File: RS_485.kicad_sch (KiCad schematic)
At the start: 17 parts, among them U6 SP3071EEN-L/TR

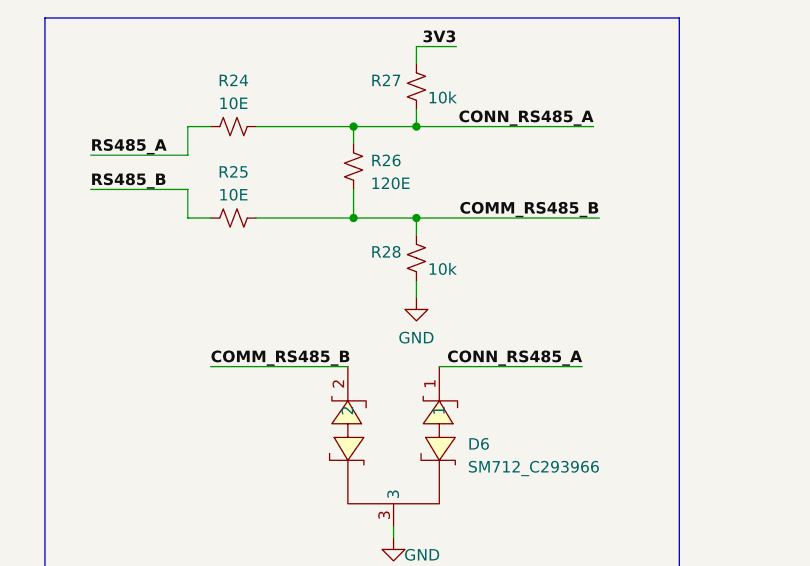
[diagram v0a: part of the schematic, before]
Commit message: Completed RS485 and CAN routing
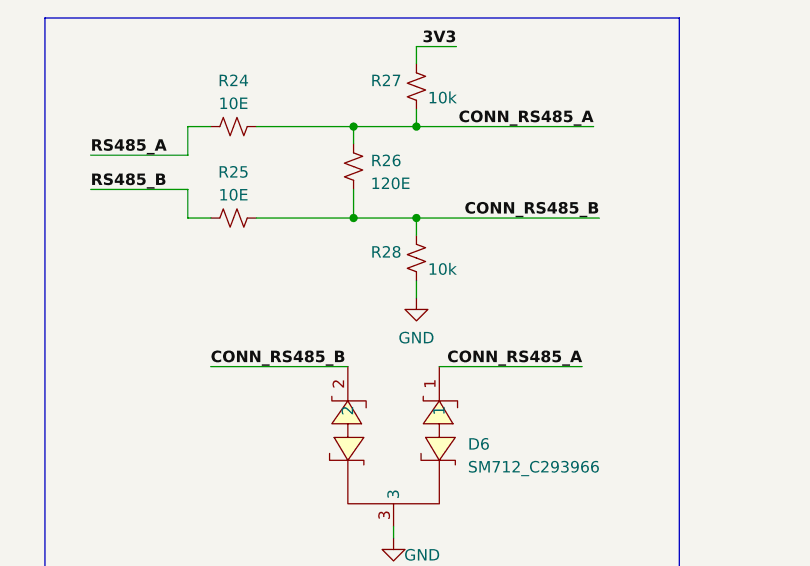
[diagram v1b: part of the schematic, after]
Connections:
- net COMM_RS485_B is gone; now on net CONN_RS485_B: D6.2, R25.2, R26.1, R28.2
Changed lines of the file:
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@@
     (effects (font (size 1.27 1.27) (thickness 0.254) bold (color 255 0 0 1)) (justify right bottom))
   )
-  (label "COMM_RS485_B" (at 262.89 81.28 180) (fields_autoplaced)
+  (label "CONN_RS485_B" (at 262.89 81.28 180) (fields_autoplaced)
     (effects (font (size 1.27 1.27) (thickness 0.254) bold (color 0 0 0 1)) (justify right bottom))
   )
@@
     (effects (font (size 1.27 1.27) (thickness 0.254) bold (color 0 0 255 1)) (justify right bottom))
   )
-  (label "COMM_RS485_B" (at 219.71 97.79 0) (fields_autoplaced)
+  (label "CONN_RS485_B" (at 219.71 97.79 0) (fields_autoplaced)
     (effects (font (size 1.27 1.27) (thickness 0.254) bold (color 0 0 0 1)) (justify left bottom))
   )

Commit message: Merge changes upstream
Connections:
- net CONN_RS485_A renamed RS485_P
- net CONN_RS485_B renamed RS485_N
- net RS485_A renamed RS_485_P
- net RS485_B renamed RS_485_N
- net RS485_~{RE}_DE renamed RS_485_~{RE}_DE
- net RS_485_DI renamed RS_485_TX
- net RS_485_RO renamed RS_485_RX
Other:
- moved on the sheet: D6

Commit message: Added HW-Tinkerers logo and supporting graphics
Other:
- company: (none) -> HW-TINKERERS (hw.tinkerers@gmail.com)
- title: (none) -> HARDWARE TINKERERS ESP32-S3 DB
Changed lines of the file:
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@@
 (kicad_sch (version 20230121) (generator eeschema)
   (paper "A4")
+  (title_block
+    (title "HARDWARE TINKERERS ESP32-S3 DB")
+    (rev "1.0.0")
+    (company "HW-TINKERERS (hw.tinkerers@gmail.com)")
+    (comment 1 "Email: bhandarkasrishtikr111@gmail.com")
+    (comment 2 "Author: Srishtik Bhandarkar")
+    (comment 3 "Email: vaibhavkhatri00@gmail.com")
+    (comment 4 "Author: Vaibhav Khatri")
+    (comment 5 "Official HW-Tinkerers email: hw.tinkerers@gmail.com")
+  )
   (junction (at 242.57 71.12) (diameter 0) (color 0 0 0 0)
   )

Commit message: Added production files for JLC (BOM and CPL)
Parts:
- C22: LCSC Part Number (none) -> C2173920
- D6: LCSC Part Number (none) -> C293966
- R13: LCSC Part Number (none) -> C95177
- R24, R25, R30, R31: LCSC Part Number (none) -> C102753
- R26: LCSC Part Number (none) -> C114758
- R27, R28, R29: LCSC Part Number (none) -> C60490
- R32, R33: LCSC Part Number (none) -> C105872
- TP1, TP2, TP5: now left out of the parts list
- U6: LCSC Part Number (none) -> C28746; PN (none) -> SP3071EEN-L/TR
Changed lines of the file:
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@@
+      (effects (font (size 1.27 1.27)) hide)
+    )
+    (property "LCSC Part Number" "C102753" (at 58.42 93.345 0)
       (effects (font (size 1.27 1.27)) hide)
     )
@@
       (effects (font (size 1.27 1.27)) hide)
     )
+    (property "LCSC Part Number" "C102753" (at 58.42 101.6 0)
+      (effects (font (size 1.27 1.27)) hide)
+    )
     (pin "1")
     (pin "2")
@@
       (effects (font (size 1.27 1.27)) hide)
     )
+    (property "LCSC Part Number" "C102753" (at 222.25 71.12 0)
+      (effects (font (size 1.27 1.27)) hide)
+    )
     (pin "1")
     (pin "2")
@@
       (effects (font (size 1.27 1.27)) hide)
     )
+    (property "LCSC Part Number" "C114758" (at 235.585 75.565 0)
+      (effects (font (size 1.27 1.27)) hide)
+    )
     (pin "1")
     (pin "2")
@@
       (effects (font (size 1.27 1.27)) hide)
     )
+    (property "LCSC Part Number" "C60490" (at 242.57 66.675 0)
+      (effects (font (size 1.27 1.27)) hide)
+    )
     (pin "1")
     (pin "2")
@@
       (effects (font (size 1.27 1.27)) hide)
     )
+    (property "LCSC Part Number" "C102753" (at 222.25 81.28 0)
+      (effects (font (size 1.27 1.27)) hide)
+    )
     (pin "1")
     (pin "2")
@@
   )
   (symbol (lib_id "ESP32-S3_DB:TestPoint_Alt") (at 46.99 101.6 0) (unit 1)
-    (in_bom yes) (on_board yes) (dnp no)
+    (in_bom no) (on_board yes) (dnp no)
     (property "Reference" "TP2" (at 42.545 98.425 0)
       (effects (font (size 1.27 1.27)) (justify left))
@@
       (effects (font (size 1.27 1.27)) hide)
     )
+    (property "Sim.Enable" "0" (at 46.99 101.6 0)
+      (effects (font (size 1.27 1.27)) hide)
+    )
     (pin "1")
     (instances
@@
       (effects (font (size 1.27 1.27)) hide)
     )
+    (property "LCSC Part Number" "C95177" (at 175.26 70.485 0)
+      (effects (font (size 1.27 1.27)) hide)
+    )
     (pin "1")
     (pin "2")
@@
       (effects (font (size 1.27 1.27)) hide)
     )
+    (property "LCSC Part Number" "C293966" (at 236.22 107.95 0)
+      (effects (font (size 1.27 1.27)) hide)
+    )
     (pin "1")
     (pin "2")
@@
     (property "Arrow Price/Stock" "https://www.arrow.com/en/products/max485esat/maxim-integrated?region=nac" (at 161.29 1080.01 0)
       (effects (font (size 1.27 1.27)) (justify left top) hide)
+    )
+    (property "LCSC Part Number" "C28746" (at 139.7 85.09 0)
+      (effects (font (size 1.27 1.27)) hide)
+    )
+    (property "PN" "SP3071EEN-L/TR" (at 139.7 85.09 0)
+      (effects (font (size 1.27 1.27)) hide)
     )
     (pin "1")
@@
       (effects (font (size 1.27 1.27)) hide)
     )
+    (property "LCSC Part Number" "C105872" (at 69.215 85.725 0)
+      (effects (font (size 1.27 1.27)) hide)
+    )
     (pin "1")
     (pin "2")
@@
       (effects (font (size 1.27 1.27)) hide)
     )
+    (property "LCSC Part Number" "C2173920" (at 170.815 76.835 0)
+      (effects (font (size 1.27 1.27)) hide)
+    )
     (pin "1")
     (pin "2")
@@
       (effects (font (size 1.27 1.27)) hide)
     )
+    (property "LCSC Part Number" "C105872" (at 62.865 85.725 0)
+      (effects (font (size 1.27 1.27)) hide)
+    )
     (pin "1")
     (pin "2")
@@
   )
   (symbol (lib_id "ESP32-S3_DB:TestPoint_Alt") (at 46.99 93.345 0) (unit 1)
-    (in_bom yes) (on_board yes) (dnp no)
+    (in_bom no) (on_board yes) (dnp no)
     (property "Reference" "TP1" (at 45.085 88.265 0)
       (effects (font (size 1.27 1.27)) (justify left))
@@
       (effects (font (size 1.27 1.27)) hide)
     )
+    (property "Sim.Enable" "0" (at 46.99 93.345 0)
+      (effects (font (size 1.27 1.27)) hide)
+    )
     (pin "1")
     (instances
@@
       (effects (font (size 1.27 1.27)) hide)
     )
+    (property "LCSC Part Number" "C60490" (at 242.57 85.725 0)
+      (effects (font (size 1.27 1.27)) hide)
+    )
     (pin "1")
     (pin "2")
@@
   )
   (symbol (lib_id "ESP32-S3_DB:TestPoint_Alt") (at 40.005 82.55 0) (unit 1)
-    (in_bom yes) (on_board yes) (dnp no)
+    (in_bom no) (on_board yes) (dnp no)
     (property "Reference" "TP5" (at 38.1 77.47 0)
       (effects (font (size 1.27 1.27)) (justify left))
@@
       (effects (font (size 1.27 1.27)) hide)
     )
+    (property "Sim.Enable" "0" (at 40.005 82.55 0)
+      (effects (font (size 1.27 1.27)) hide)
+    )
     (pin "1")
     (instances
@@
       (effects (font (size 1.27 1.27)) hide)
     )
+    (property "LCSC Part Number" "C60490" (at 116.205 98.425 0)
+      (effects (font (size 1.27 1.27)) hide)
+    )
